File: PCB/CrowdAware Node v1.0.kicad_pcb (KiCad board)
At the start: 2 copper layers, 61 x 36.5 mm, 10 parts, among them J1 Heltec WiFi LoRa 32(V3)

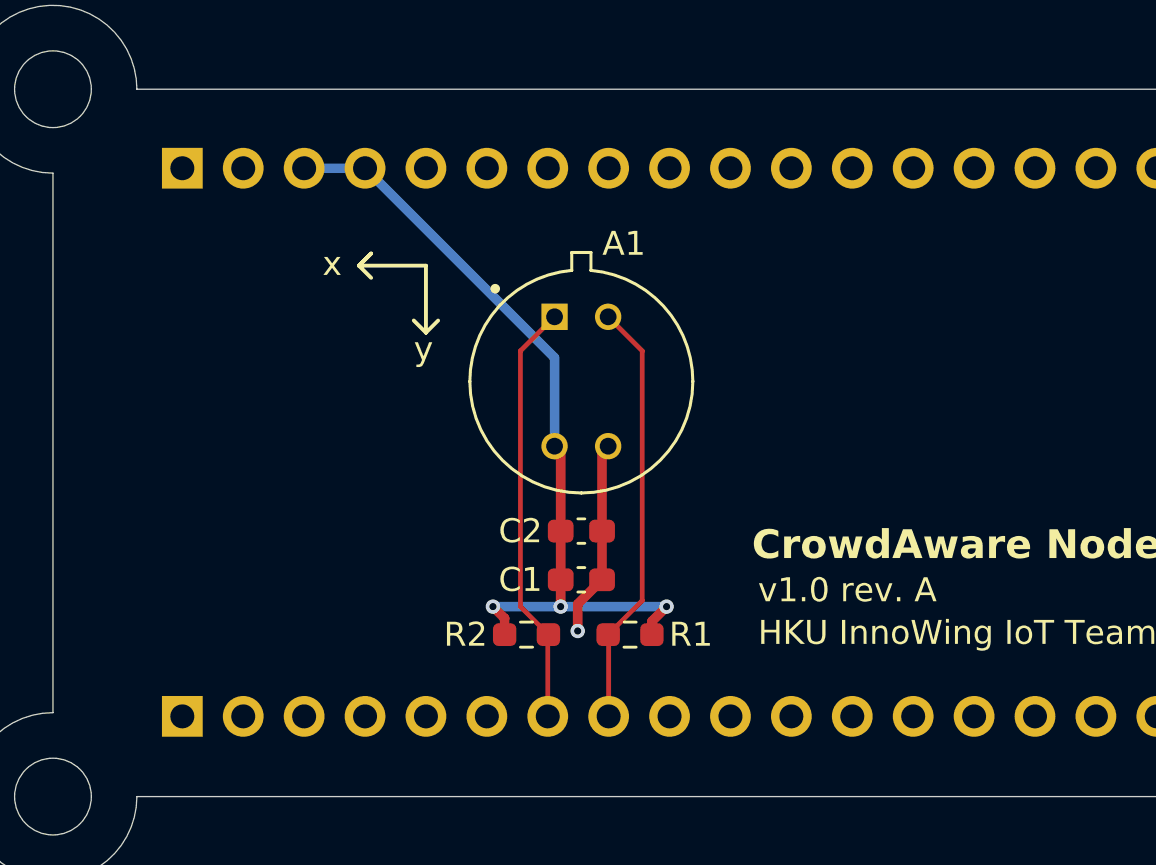
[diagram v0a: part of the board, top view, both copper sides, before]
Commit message: Revised routing, changed pullup to 3v3
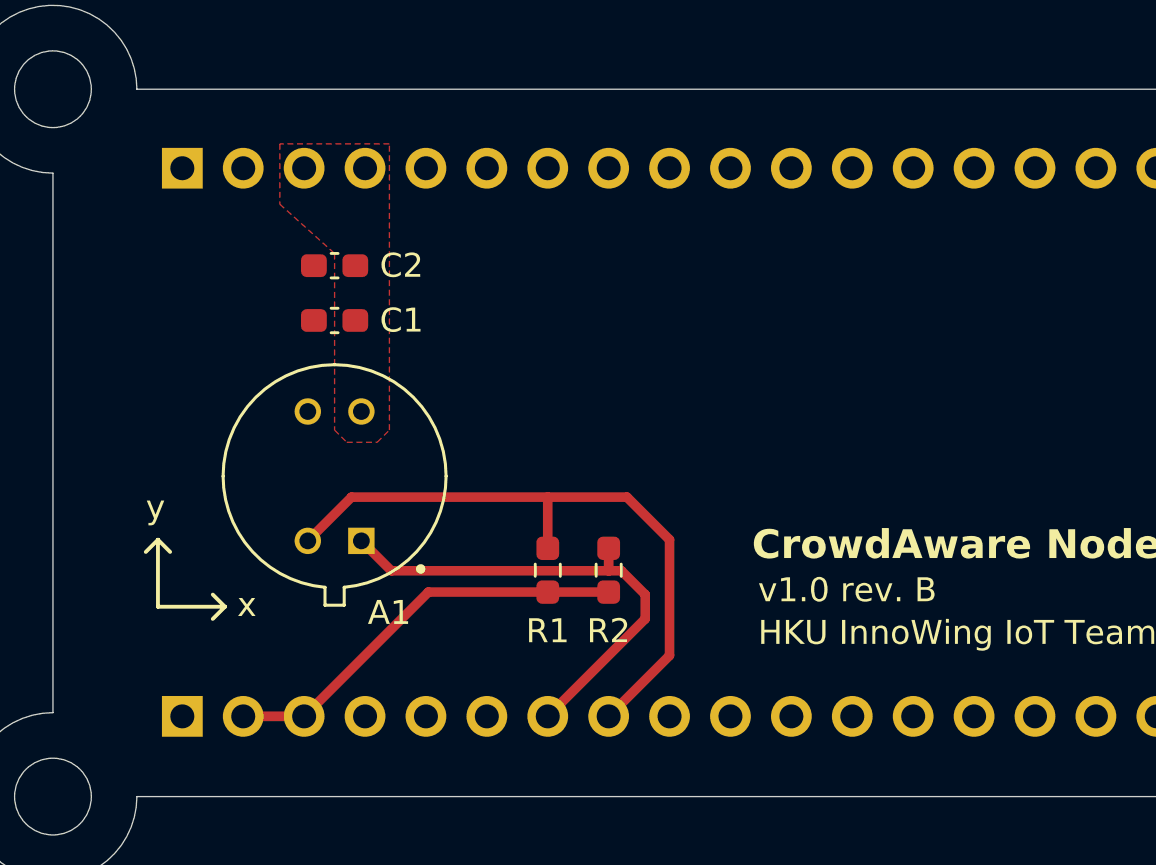
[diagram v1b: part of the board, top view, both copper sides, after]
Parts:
- moved C2 15.1 mm to (88.9, 65.5), turned to 180 degrees
- moved C1 14.9 mm to (88.9, 67.8), turned to 180 degrees
- moved A1 11.0 mm to (88.9, 74.3), turned to 157.5 degrees
- moved R1 4.36 mm to (97.8, 78.2), turned to 90 degrees
- moved R2 4.35 mm to (100.3, 78.2), turned to 90 degrees
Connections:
- A1 pad 2: +3V3 -> V_EXT
- C1 pad 1: +3V3 -> V_EXT
- C2 pad 1: +3V3 -> V_EXT
- J1 pad 30: +3V3 -> V_EXT
- J1 pad 31: unconnected-(J1-Pin_31-Pad31) -> +3V3
- J1 pad 32: +3V3 -> V_EXT
- J1 pad 33: unconnected-(J1-Pin_33-Pad33) -> +3V3
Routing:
- net +3V3: track 34.2 -> 17.4 mm, vias 3 -> 0
- net /SCL: track 17.8 -> 27.1 mm
- net GND: track 8.23 -> 0.00 mm, vias 1 -> 0
- net /SDA: track 17.7 -> 20.5 mm
- added copper zone on F.Cu, net V_EXT
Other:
- board text added: "3V3"
- board text added: "USB"
- board text added: "v1.0 rev. B"
- board text removed: "v1.0 rev. A"

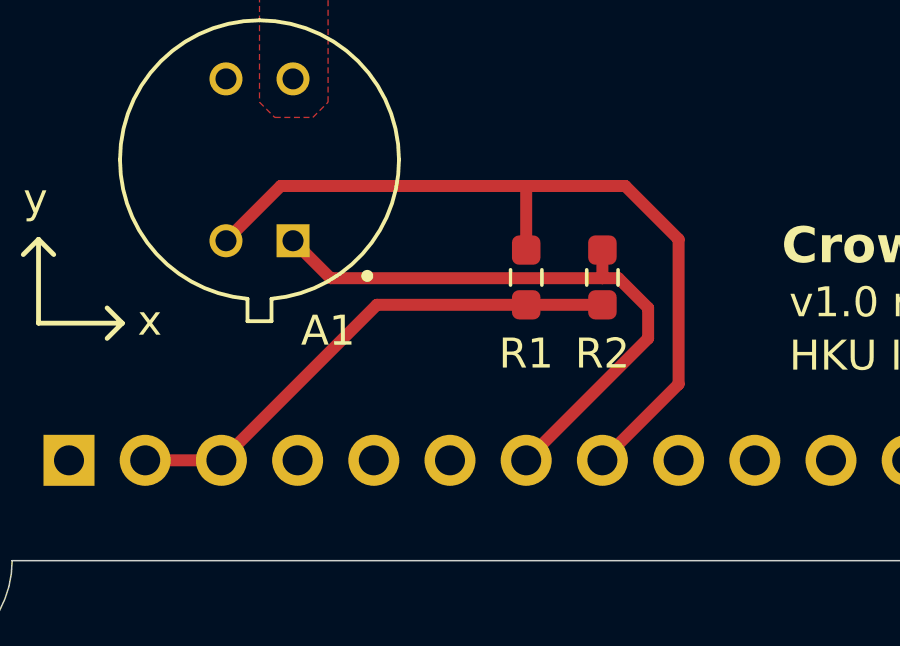
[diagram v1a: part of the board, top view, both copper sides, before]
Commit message: Minor adjustment to trace spacing
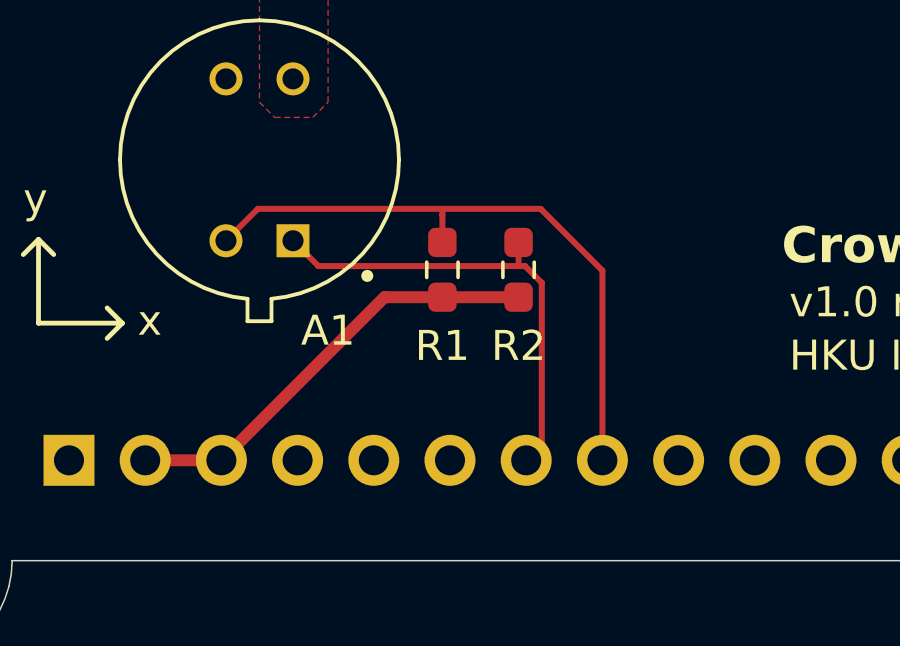
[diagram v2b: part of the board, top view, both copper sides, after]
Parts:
- moved R1 2.81 mm to (95.0, 78.0)
- moved R2 2.81 mm to (97.5, 78.0)
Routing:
- net /SCL: track 27.1 -> 21.3 mm
- net /SDA: track 20.5 -> 15.8 mm
- net +3V3: track 17.4 -> 14.7 mm
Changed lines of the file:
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@@
 		)
 		(pad "2" thru_hole circle
-			(at -0.000001 2.919999 157.5)
+			(at -0.000001 2.919999 180)
 			(size 1.1 1.1)
 			(drill 0.7)
@@
 	(footprint "MyLib:R_0603_1608Metric_Pad0.98x0.95mm_HandSolder"
 		(layer "F.Cu")
-		(at 97.79 78.232 90)
+		(at 94.996 77.978 90)
 		(descr "Resistor SMD 0603 (1608 Metric), square (rectangular) end terminal, IPC-7351 nominal with elongated pad for handsoldering. (Body size source: IPC-SM-782 page 72, https://www.pcb-3d.com/wordpress/wp-content/uploads/ipc-sm-782a_amendment_1_and_2.pdf), generated with kicad-footprint-generator")
 		(tags "resistor handsolder")
@@
 	(footprint "MyLib:R_0603_1608Metric_Pad0.98x0.95mm_HandSolder"
 		(layer "F.Cu")
-		(at 100.33 78.232 90)
+		(at 97.536 77.978 90)
 		(descr "Resistor SMD 0603 (1608 Metric), square (rectangular) end terminal, IPC-7351 nominal with elongated pad for handsoldering. (Body size source: IPC-SM-782 page 72, https://www.pcb-3d.com/wordpress/wp-content/uploads/ipc-sm-782a_amendment_1_and_2.pdf), generated with kicad-footprint-generator")
 		(tags "resistor handsolder")
@@
 	)
 	(segment
-		(start 100.863 78.257)
-		(end 101.854 79.248)
-		(width 0.4)
+		(start 97.536 77.853)
+		(end 97.752722 77.853)
+		(width 0.2)
+		(layer "F.Cu")
+		(net "/SDA")
+	)
+	(segment
+		(start 97.752722 77.853)
+		(end 98.311 78.411278)
+		(width 0.2)
+		(layer "F.Cu")
+		(net "/SDA")
+	)
+	(segment
+		(start 90.861709 77.853)
+		(end 97.536 77.853)
+		(width 0.2)
+		(layer "F.Cu")
+		(net "/SDA")
+	)
+	(segment
+		(start 97.536 77.853)
+		(end 97.536 77.0655)
+		(width 0.2)
 		(layer "F.Cu")
 		(net "/SDA")
@@
 	(segment
 		(start 90.017434 77.008725)
-		(end 91.265709 78.257)
-		(width 0.4)
+		(end 90.861709 77.853)
+		(width 0.2)
 		(layer "F.Cu")
 		(net "/SDA")
 	)
 	(segment
-		(start 100.33 78.257)
-		(end 100.33 77.3195)
-		(width 0.4)
+		(start 98.311 78.411278)
+		(end 98.311 83.807)
+		(width 0.2)
 		(layer "F.Cu")
 		(net "/SDA")
 	)
 	(segment
-		(start 91.265709 78.257)
-		(end 100.33 78.257)
-		(width 0.4)
+		(start 98.311 83.807)
+		(end 97.79 84.328)
+		(width 0.2)
 		(layer "F.Cu")
 		(net "/SDA")
 	)
 	(segment
-		(start 101.854 80.264)
-		(end 97.79 84.328)
-		(width 0.4)
-		(layer "F.Cu")
-		(net "/SDA")
+		(start 94.996 75.946)
+		(end 94.996 76.158725)
+		(width 0.2)
+		(layer "F.Cu")
+		(net "/SCL")
 	)
 	(segment
-		(start 101.854 79.248)
-		(end 101.854 80.264)
-		(width 0.4)
-		(layer "F.Cu")
-		(net "/SDA")
+		(start 100.33 78.004086)
+		(end 100.33 84.328)
+		(width 0.2)
+		(layer "F.Cu")
+		(net "/SCL")
 	)
 	(segment
-		(start 100.33 78.257)
-		(end 100.863 78.257)
-		(width 0.4)
-		(layer "F.Cu")
-		(net "/SDA")
+		(start 94.996 75.946)
+		(end 98.271914 75.946)
+		(width 0.2)
+		(layer "F.Cu")
+		(net "/SCL")
 	)
 	(segment
-		(start 97.79 75.184)
-		(end 101.092 75.184)
-		(width 0.4)
+		(start 94.996 77.0655)
+		(end 94.996 76.158725)
+		(width 0.2)
 		(layer "F.Cu")
 		(net "/SCL")
 	)
 	(segment
-		(start 97.79 77.3195)
-		(end 97.79 75.184)
-		(width 0.4)
+		(start 88.845291 75.946)
+		(end 94.996 75.946)
+		(width 0.2)
 		(layer "F.Cu")
 		(net "/SCL")
 	)
 	(segment
-		(start 89.607291 75.184)
-		(end 97.79 75.184)
-		(width 0.4)
-		(layer "F.Cu")
-		(net "/SCL")
-	)
-	(segment
-		(start 102.87 81.788)
-		(end 100.33 84.328)
-		(width 0.4)
-		(layer "F.Cu")
-		(net "/SCL")
-	)
-	(segment
-		(start 101.092 75.184)
-		(end 102.87 76.962)
-		(width 0.4)
+		(start 98.271914 75.946)
+		(end 100.33 78.004086)
+		(width 0.2)
 		(layer "F.Cu")
 		(net "/SCL")
@@
 	(segment
 		(start 87.782564 77.008727)
-		(end 89.607291 75.184)
-		(width 0.4)
+		(end 88.845291 75.946)
+		(width 0.2)
 		(layer "F.Cu")
 		(net "/SCL")
-	)
-	(segment
-		(start 102.87 76.962)
-		(end 102.87 81.788)
-		(width 0.4)
-		(layer "F.Cu")
-		(net "/SCL")
-	)
-	(segment
-		(start 100.33 79.1445)
-		(end 92.8135 79.1445)
-		(width 0.4)
-		(layer "F.Cu")
-		(net "+3V3")
-	)
-	(segment
-		(start 92.8135 79.1445)
-		(end 87.63 84.328)
-		(width 0.4)
-		(layer "F.Cu")
-		(net "+3V3")
 	)
 	(segment
@@
 		(width 0.4)
 		(layer "F.Cu")
+		(net "+3V3")
+	)
+	(segment
+		(start 93.0675 78.8905)
+		(end 97.536 78.8905)
+		(width 0.4)
+		(layer "F.Cu")
+		(net "+3V3")
+	)
+	(segment
+		(start 87.63 84.328)
+		(end 93.0675 78.8905)
+		(width 0.4)
+		(layer "F.Cu")
